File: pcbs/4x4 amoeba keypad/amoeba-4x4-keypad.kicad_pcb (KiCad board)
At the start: 2 copper layers, 75.9 x 74.5 mm, 105 parts, among them U1 ProMicro-18mil-offset

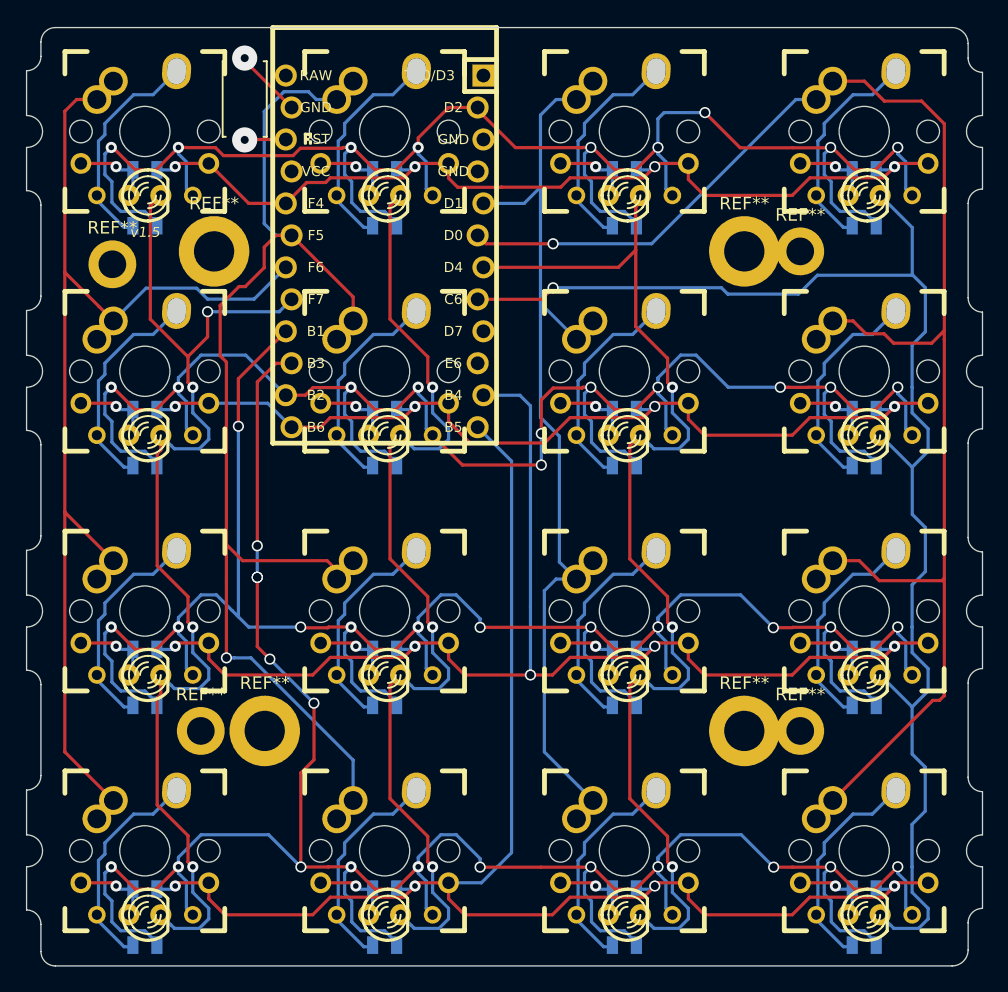
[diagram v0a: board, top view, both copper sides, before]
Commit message: fix zone filling
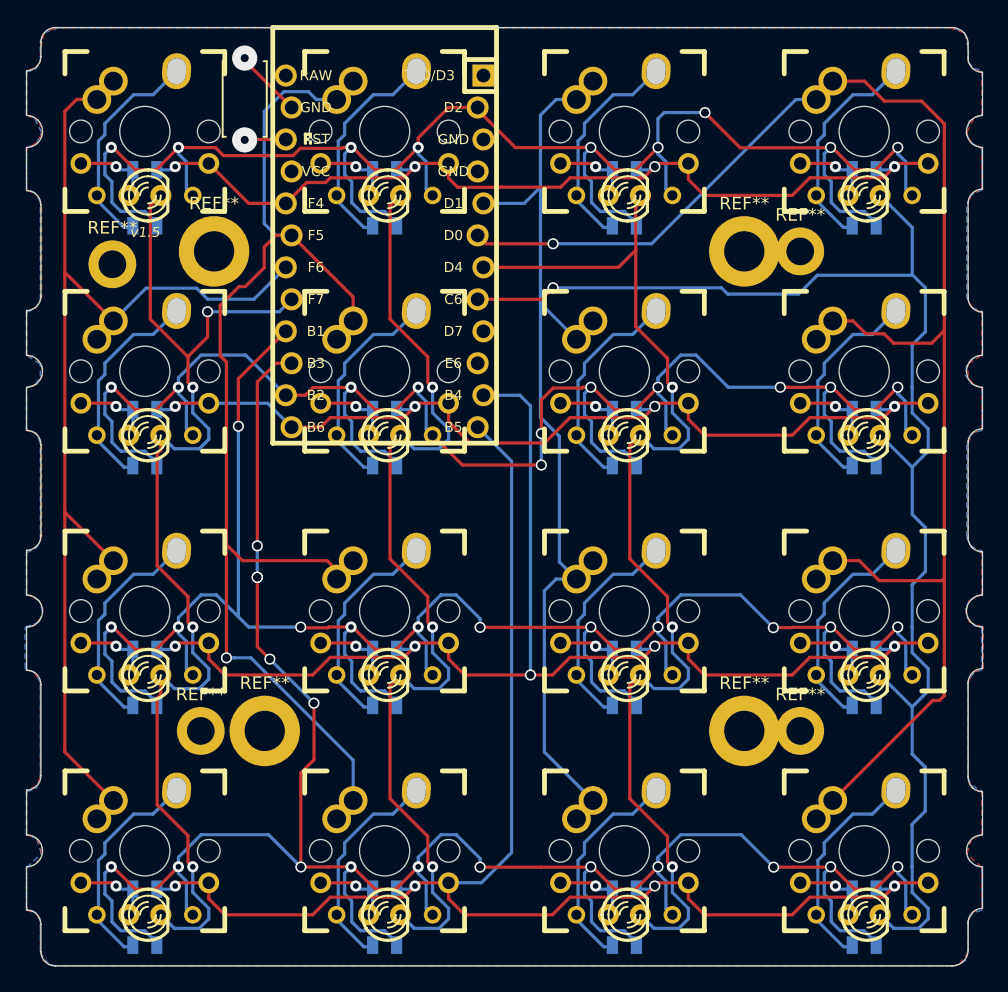
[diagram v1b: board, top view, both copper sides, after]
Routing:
- added copper zone on B.Cu, net (none)
- added copper zone on F.Cu, net (none)
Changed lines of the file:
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@@
     (0 F.Cu signal)
     (31 B.Cu signal)
-    (32 B.Adhes user hide)
-    (33 F.Adhes user hide)
-    (34 B.Paste user hide)
-    (35 F.Paste user hide)
-    (36 B.SilkS user hide)
+    (32 B.Adhes user)
+    (33 F.Adhes user)
+    (34 B.Paste user)
+    (35 F.Paste user)
+    (36 B.SilkS user)
     (37 F.SilkS user)
-    (38 B.Mask user hide)
-    (39 F.Mask user hide)
-    (40 Dwgs.User user hide)
-    (41 Cmts.User user hide)
-    (42 Eco1.User user hide)
-    (43 Eco2.User user hide)
+    (38 B.Mask user)
+    (39 F.Mask user)
+    (40 Dwgs.User user)
+    (41 Cmts.User user)
+    (42 Eco1.User user)
+    (43 Eco2.User user)
     (44 Edge.Cuts user)
   )
@@
     (solder_mask_min_width 0.25)
     (aux_axis_origin 0 0)
-    (grid_origin 314.325 123.698)
+    (grid_origin 239.522 105.664)
     (visible_elements 7FFFFFFF)
     (pcbplotparams
-      (layerselection 0x00030_ffffffff)
+      (layerselection 0x010fd_ffffffff)
       (usegerberextensions true)
       (usegerberattributes false)
@@
   (segment (start 245.11 172.72) (end 245.236998 172.593002) (width 0.254) (layer B.Cu) (net 0))
   (segment (start 245.745 167.005) (end 245.745 167.894) (width 0.254) (layer B.Cu) (net 0))
-  (via (at 280.42 136.99) (size 0.889) (drill 0.635) (layers F.Cu B.Cu) (net 13))
-  (via (at 256.853 111.16) (size 2) (drill 0.635) (layers F.Cu B.Cu) (net 20))
-  (via (at 256.853 104.66) (size 2) (drill 0.635) (layers F.Cu B.Cu) (net 19))
   (via (at 252.73 130.81) (size 0.889) (layers F.Cu B.Cu) (net 1))
   (segment (start 252.730002 130.810002) (end 252.730002 132.842002) (width 0.254) (layer B.Cu) (net 1))
@@
   (segment (start 302.26 107.95) (end 300.643554 107.95) (width 0.254) (layer B.Cu) (net 12))
   (segment (start 300.643554 107.95) (end 289.183554 119.41) (width 0.254) (layer B.Cu) (net 12))
+  (via (at 280.42 136.99) (size 0.889) (drill 0.635) (layers F.Cu B.Cu) (net 13))
   (via (at 251.587 130.81) (size 0.889) (layers F.Cu B.Cu) (net 13))
   (via (at 246.253 130.81) (size 0.889) (layers F.Cu B.Cu) (net 13))
@@
   (segment (start 275.659 170.18) (end 273.05 170.18) (width 0.254) (layer B.Cu) (net 18))
   (segment (start 278.055 167.784) (end 275.659 170.18) (width 0.254) (layer B.Cu) (net 18))
+  (via (at 256.853 104.66) (size 2) (drill 0.635) (layers F.Cu B.Cu) (net 19))
   (segment (start 256.853 104.8594) (end 256.853 104.66) (width 0.254) (layer F.Cu) (net 19))
   (segment (start 260.5786 108.585) (end 256.853 104.8594) (width 0.254) (layer F.Cu) (net 19))
+  (via (at 256.853 111.16) (size 2) (drill 0.635) (layers F.Cu B.Cu) (net 20))
   (segment (start 256.888 111.125) (end 256.853 111.16) (width 0.254) (layer F.Cu) (net 20))
   (segment (start 260.1214 111.125) (end 256.888 111.125) (width 0.254) (layer F.Cu) (net 20))
+  (zone (net 0) (net_name "") (layer F.Cu) (hatch edge 0.508)
+    (connect_pads (clearance 0.508))
+    (min_thickness 0.254)
+    (fill yes (arc_segments 16) (thermal_gap 0.508) (thermal_bridge_width 0.508))
+    (polygon
+      (pts
+        (xy 239.522 105.664) (xy 239.522 109.164) (xy 240.522 109.664) (xy 240.772 110.664) (xy 240.272 111.414)
+        (xy 239.522 111.914) (xy 239.522 115.164) (xy 240.122 115.364) (xy 240.522 115.764) (xy 240.722 116.464)
+        (xy 240.722 123.664) (xy 240.322 124.464) (xy 239.522 124.764) (xy 239.522 128.264) (xy 240.222 128.464)
+        (xy 240.722 129.064) (xy 240.822 129.864) (xy 240.322 130.564) (xy 239.522 130.864) (xy 239.522 134.264)
+        (xy 240.122 134.364) (xy 240.522 134.764) (xy 240.722 135.364) (xy 240.722 142.764) (xy 240.422 143.364)
+        (xy 239.822 143.764) (xy 239.522 143.764) (xy 239.522 147.264) (xy 240.022 147.464) (xy 240.522 147.764)
+        (xy 240.822 148.364) (xy 240.722 149.064) (xy 240.122 149.764) (xy 239.522 149.864) (xy 239.522 153.264)
+        (xy 240.122 153.464) (xy 240.622 154.164) (xy 240.622 154.664) (xy 240.622 161.764) (xy 240.322 162.464)
+        (xy 239.522 162.864) (xy 239.522 166.364) (xy 240.322 166.664) (xy 240.722 167.364) (xy 240.622 168.264)
+        (xy 240.122 168.764) (xy 239.522 168.964) (xy 239.522 172.364) (xy 240.222 172.564) (xy 240.622 173.164)
+        (xy 240.622 175.564) (xy 240.822 176.364) (xy 241.622 176.764) (xy 313.122 176.764) (xy 313.622 176.664)
+        (xy 314.222 175.864) (xy 314.322 175.564) (xy 314.322 173.264) (xy 314.622 172.564) (xy 315.422 172.164)
+        (xy 315.422 168.964) (xy 314.222 167.864) (xy 314.622 166.664) (xy 315.422 166.364) (xy 315.422 162.964)
+        (xy 314.622 162.664) (xy 314.322 161.764) (xy 314.322 154.264) (xy 314.722 153.464) (xy 315.522 153.164)
+        (xy 315.522 149.864) (xy 314.422 149.464) (xy 314.122 148.664) (xy 314.422 147.764) (xy 315.422 147.264)
+        (xy 315.422 143.964) (xy 314.622 143.564) (xy 314.322 142.964) (xy 314.322 135.264) (xy 314.622 134.464)
+        (xy 315.422 134.164) (xy 315.422 130.864) (xy 314.722 130.564) (xy 314.322 129.964) (xy 314.322 128.964)
+        (xy 315.422 128.264) (xy 315.422 124.864) (xy 314.722 124.564) (xy 314.322 123.864) (xy 314.322 116.064)
+        (xy 314.722 115.364) (xy 315.422 115.064) (xy 315.422 111.764) (xy 314.622 111.464) (xy 314.222 110.564)
+        (xy 314.822 109.364) (xy 315.422 109.164) (xy 315.422 105.764) (xy 314.722 105.564) (xy 314.322 104.964)
+        (xy 314.322 103.364) (xy 314.022 102.664) (xy 312.922 102.264) (xy 241.722 102.264) (xy 240.922 102.664)
+        (xy 240.622 104.064) (xy 240.622 104.964) (xy 240.122 105.464)
+      )
+    )
+  )
+  (zone (net 0) (net_name "") (layer B.Cu) (hatch edge 0.508)
+    (connect_pads (clearance 0.508))
+    (min_thickness 0.254)
+    (fill yes (arc_segments 16) (thermal_gap 0.508) (thermal_bridge_width 0.508))
+    (polygon
+      (pts
+        (xy 315.412437 105.664) (xy 315.412437 109.164) (xy 314.412437 109.664) (xy 314.162437 110.664) (xy 314.662437 111.414)
+        (xy 315.412437 111.914) (xy 315.412437 115.164) (xy 314.812437 115.364) (xy 314.412437 115.764) (xy 314.212437 116.464)
+        (xy 314.212437 123.664) (xy 314.612437 124.464) (xy 315.412437 124.764) (xy 315.412437 128.264) (xy 314.712437 128.464)
+        (xy 314.212437 129.064) (xy 314.112437 129.864) (xy 314.612437 130.564) (xy 315.412437 130.864) (xy 315.412437 134.264)
+        (xy 314.812437 134.364) (xy 314.412437 134.764) (xy 314.212437 135.364) (xy 314.212437 142.764) (xy 314.512437 143.364)
+        (xy 315.112437 143.764) (xy 315.412437 143.764) (xy 315.412437 147.264) (xy 314.912437 147.464) (xy 314.412437 147.764)
+        (xy 314.112437 148.364) (xy 314.212437 149.064) (xy 314.812437 149.764) (xy 315.412437 149.864) (xy 315.412437 153.264)
+        (xy 314.812437 153.464) (xy 314.312437 154.164) (xy 314.312437 154.664) (xy 314.312437 161.764) (xy 314.612437 162.464)
+        (xy 315.412437 162.864) (xy 315.412437 166.364) (xy 314.612437 166.664) (xy 314.212437 167.364) (xy 314.312437 168.264)
+        (xy 314.812437 168.764) (xy 315.412437 168.964) (xy 315.412437 172.364) (xy 314.712437 172.564) (xy 314.312437 173.164)
+        (xy 314.312437 175.564) (xy 314.112437 176.364) (xy 313.312437 176.764) (xy 241.812437 176.764) (xy 241.312437 176.664)
+        (xy 240.712437 175.864) (xy 240.612437 175.564) (xy 240.612437 173.264) (xy 240.312437 172.564) (xy 239.512437 172.164)
+        (xy 239.512437 168.964) (xy 240.712437 167.864) (xy 240.312437 166.664) (xy 239.512437 166.364) (xy 239.512437 162.964)
+        (xy 240.312437 162.664) (xy 240.612437 161.764) (xy 240.612437 154.264) (xy 240.212437 153.464) (xy 239.412437 153.164)
+        (xy 239.412437 149.864) (xy 240.512437 149.464) (xy 240.812437 148.664) (xy 240.512437 147.764) (xy 239.512437 147.264)
+        (xy 239.512437 143.964) (xy 240.312437 143.564) (xy 240.612437 142.964) (xy 240.612437 135.264) (xy 240.312437 134.464)
+        (xy 239.512437 134.164) (xy 239.512437 130.864) (xy 240.212437 130.564) (xy 240.612437 129.964) (xy 240.612437 128.964)
+        (xy 239.512437 128.264) (xy 239.512437 124.864) (xy 240.212437 124.564) (xy 240.612437 123.864) (xy 240.612437 116.064)
+        (xy 240.212437 115.364) (xy 239.512437 115.064) (xy 239.512437 111.764) (xy 240.312437 111.464) (xy 240.712437 110.564)
+        (xy 240.112437 109.364) (xy 239.512437 109.164) (xy 239.512437 105.764) (xy 240.212437 105.564) (xy 240.612437 104.964)
+        (xy 240.612437 103.364) (xy 240.912437 102.664) (xy 242.012437 102.264) (xy 313.212437 102.264) (xy 314.072 102.664)
+        (xy 314.372 104.064) (xy 314.312437 104.964) (xy 314.812437 105.464)
+      )
+    )
+  )
 )
